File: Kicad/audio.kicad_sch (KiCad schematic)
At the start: 39 parts, among them J801 Conn_01x04, J802 Conn_02x05, J803 Conn_01x04, U801 TLV320AIC23BPW, U802 STX-4335-5BGP-S1, Y801 12M 20pF

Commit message: Label adjustments.
Swap 10uF to 10u (the F is implied)
Adjust some left/right alignment and nudge some labels around
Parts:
- C801, C808, C809: value 100uF -> 100u
- C802, C803, C806, C807, C815: value 10uF -> 10u
- C804, C805, C810, C811, C818: value 1uF -> 1u
- C812, C813, C819: value 47pF -> 47p
- C814: value 100nF -> 100n
- C816, C817: value 22pF -> 22p
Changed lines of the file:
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@@
       (effects (font (size 1.27 1.27)) (justify left))
     )
-    (property "Value" "10uF" (id 1) (at 64.135 33.02 0)
+    (property "Value" "10u" (id 1) (at 64.135 33.02 0)
       (effects (font (size 1.27 1.27)) (justify left))
     )
@@
       (effects (font (size 1.27 1.27)) (justify left))
     )
-    (property "Value" "10uF" (id 1) (at 52.705 33.02 0)
+    (property "Value" "10u" (id 1) (at 52.705 33.02 0)
       (effects (font (size 1.27 1.27)) (justify left))
     )
@@
       (effects (font (size 1.27 1.27)) (justify left))
     )
-    (property "Value" "10uF" (id 1) (at 42.291 52.578 0)
+    (property "Value" "10u" (id 1) (at 42.291 52.578 0)
       (effects (font (size 1.27 1.27)) (justify left))
     )
@@
       (effects (font (size 1.27 1.27)) (justify left))
     )
-    (property "Value" "10uF" (id 1) (at 104.14 111.76 0)
+    (property "Value" "10u" (id 1) (at 104.14 111.76 0)
       (effects (font (size 1.27 1.27)) (justify left))
     )
@@
       (effects (font (size 1.27 1.27)) (justify left))
     )
-    (property "Value" "100nF" (id 1) (at 92.71 111.76 0)
+    (property "Value" "100n" (id 1) (at 92.71 111.76 0)
       (effects (font (size 1.27 1.27)) (justify left))
     )
@@
       (effects (font (size 1.27 1.27)) (justify right))
     )
-    (property "Value" "22pF" (id 1) (at 36.83 121.285 0)
+    (property "Value" "22p" (id 1) (at 36.83 121.285 0)
       (effects (font (size 1.27 1.27)) (justify right))
     )
@@
       (effects (font (size 1.27 1.27)) (justify left))
     )
-    (property "Value" "22pF" (id 1) (at 48.26 121.285 0)
+    (property "Value" "22p" (id 1) (at 48.26 121.285 0)
       (effects (font (size 1.27 1.27)) (justify left))
     )
@@
     (in_bom yes) (on_board yes)
     (property "Reference" "C808" (id 0) (at 134.62 56.515 90))
-    (property "Value" "100uF" (id 1) (at 134.62 58.8264 90))
+    (property "Value" "100u" (id 1) (at 134.62 58.8264 90))
     (property "Footprint" "Capacitor_THT:CP_Radial_D8.0mm_P5.00mm" (id 2) (at 134.62 62.23 0)
       (effects (font (size 1.27 1.27)) hide)
@@
       (effects (font (size 1.27 1.27)) (justify right))
     )
-    (property "Value" "47pF" (id 1) (at 184.5818 128.778 0)
+    (property "Value" "47p" (id 1) (at 184.5818 128.778 0)
       (effects (font (size 1.27 1.27)) (justify right))
     )
@@
     (in_bom yes) (on_board yes)
     (property "Reference" "C818" (id 0) (at 158.75 127 90))
-    (property "Value" "1uF" (id 1) (at 158.75 129.54 90))
+    (property "Value" "1u" (id 1) (at 158.75 129.54 90))
     (property "Footprint" "Capacitor_SMD:C_0805_2012Metric_Pad1.18x1.45mm_HandSolder" (id 2) (at 158.75 123.19 0)
       (effects (font (size 1.27 1.27)) hide)
@@
     (in_bom yes) (on_board yes)
     (property "Reference" "C811" (id 0) (at 134.62 99.06 90))
-    (property "Value" "1uF" (id 1) (at 134.62 101.6 90))
+    (property "Value" "1u" (id 1) (at 134.62 101.6 90))
     (property "Footprint" "Capacitor_SMD:C_0805_2012Metric_Pad1.18x1.45mm_HandSolder" (id 2) (at 134.62 95.25 0)
       (effects (font (size 1.27 1.27)) hide)
@@
     (in_bom yes) (on_board yes)
     (property "Reference" "C805" (id 0) (at 134.62 41.91 90))
-    (property "Value" "1uF" (id 1) (at 134.62 39.37 90))
+    (property "Value" "1u" (id 1) (at 134.62 39.37 90))
     (property "Footprint" "Capacitor_SMD:C_0805_2012Metric_Pad1.18x1.45mm_HandSolder" (id 2) (at 134.62 35.56 0)
       (effects (font (size 1.27 1.27)) hide)
@@
       (effects (font (size 1.27 1.27)) (justify right))
     )
-    (property "Value" "47pF" (id 1) (at 157.2768 100.203 0)
+    (property "Value" "47p" (id 1) (at 157.2768 100.203 0)
       (effects (font (size 1.27 1.27)) (justify right))
     )
@@
       (effects (font (size 1.27 1.27)) (justify right))
     )
-    (property "Value" "47pF" (id 1) (at 147.7518 100.203 0)
+    (property "Value" "47p" (id 1) (at 147.7518 100.203 0)
       (effects (font (size 1.27 1.27)) (justify right))
     )
@@
       (effects (font (size 1.27 1.27)) (justify left))
     )
-    (property "Value" "100uF" (id 1) (at 41.275 33.02 0)
+    (property "Value" "100u" (id 1) (at 41.275 33.02 0)
       (effects (font (size 1.27 1.27)) (justify left))
     )
@@
     (in_bom yes) (on_board yes)
     (property "Reference" "C809" (id 0) (at 134.62 71.755 90))
-    (property "Value" "100uF" (id 1) (at 134.62 69.215 90))
+    (property "Value" "100u" (id 1) (at 134.62 69.215 90))
     (property "Footprint" "Capacitor_THT:CP_Radial_D8.0mm_P5.00mm" (id 2) (at 134.62 66.04 0)
       (effects (font (size 1.27 1.27)) hide)
@@
     (in_bom yes) (on_board yes)
     (property "Reference" "C810" (id 0) (at 134.62 86.36 90))
-    (property "Value" "1uF" (id 1) (at 134.62 88.265 90))
+    (property "Value" "1u" (id 1) (at 134.62 88.265 90))
     (property "Footprint" "Capacitor_SMD:C_0805_2012Metric_Pad1.18x1.45mm_HandSolder" (id 2) (at 134.62 91.44 0)
       (effects (font (size 1.27 1.27)) hide)
@@
     (in_bom yes) (on_board yes)
     (property "Reference" "C804" (id 0) (at 134.62 25.4 90))
-    (property "Value" "1uF" (id 1) (at 134.62 27.94 90))
+    (property "Value" "1u" (id 1) (at 134.62 27.94 90))
     (property "Footprint" "Capacitor_SMD:C_0805_2012Metric_Pad1.18x1.45mm_HandSolder" (id 2) (at 134.62 31.75 0)
       (effects (font (size 1.27 1.27)) hide)
@@
       (effects (font (size 1.27 1.27)) (justify left))
     )
-    (property "Value" "10uF" (id 1) (at 53.086 52.578 0)
-      (effects (font (size 1.27 1.27)) (justify left))
-    )
+    (property "Value" "10u" (id 1) (at 53.086 52.578 0)
+      (effects (font (size 1.27 1.27)) (justify left))
+    )

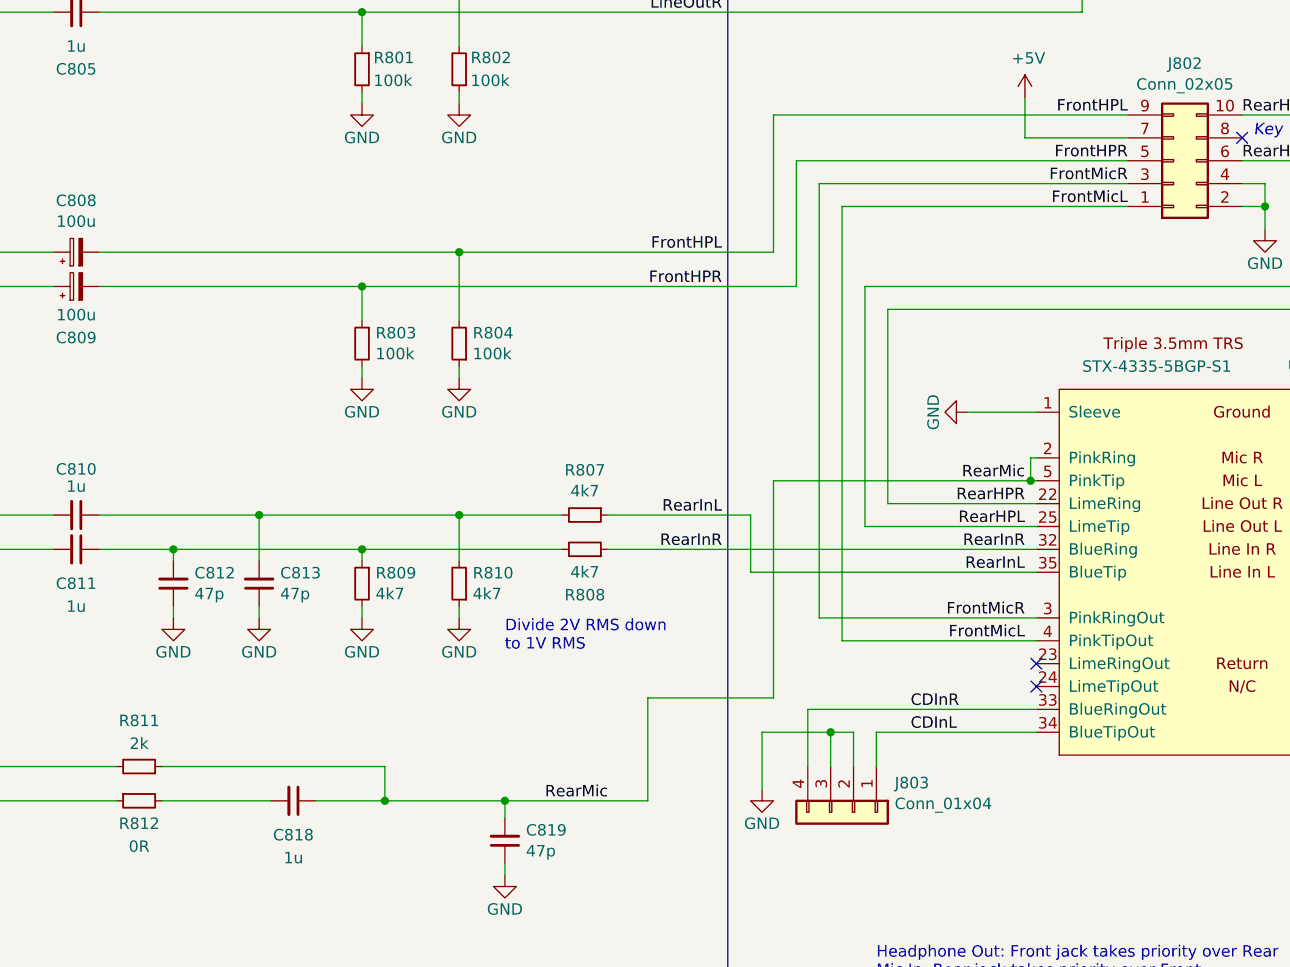
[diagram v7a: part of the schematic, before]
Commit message: Fix mic/bias circuit.
Also:

* added MOV as 3D model for fuse
* re-routed bottom side 5V line
* added some GND vias near power vias to reduce loop area
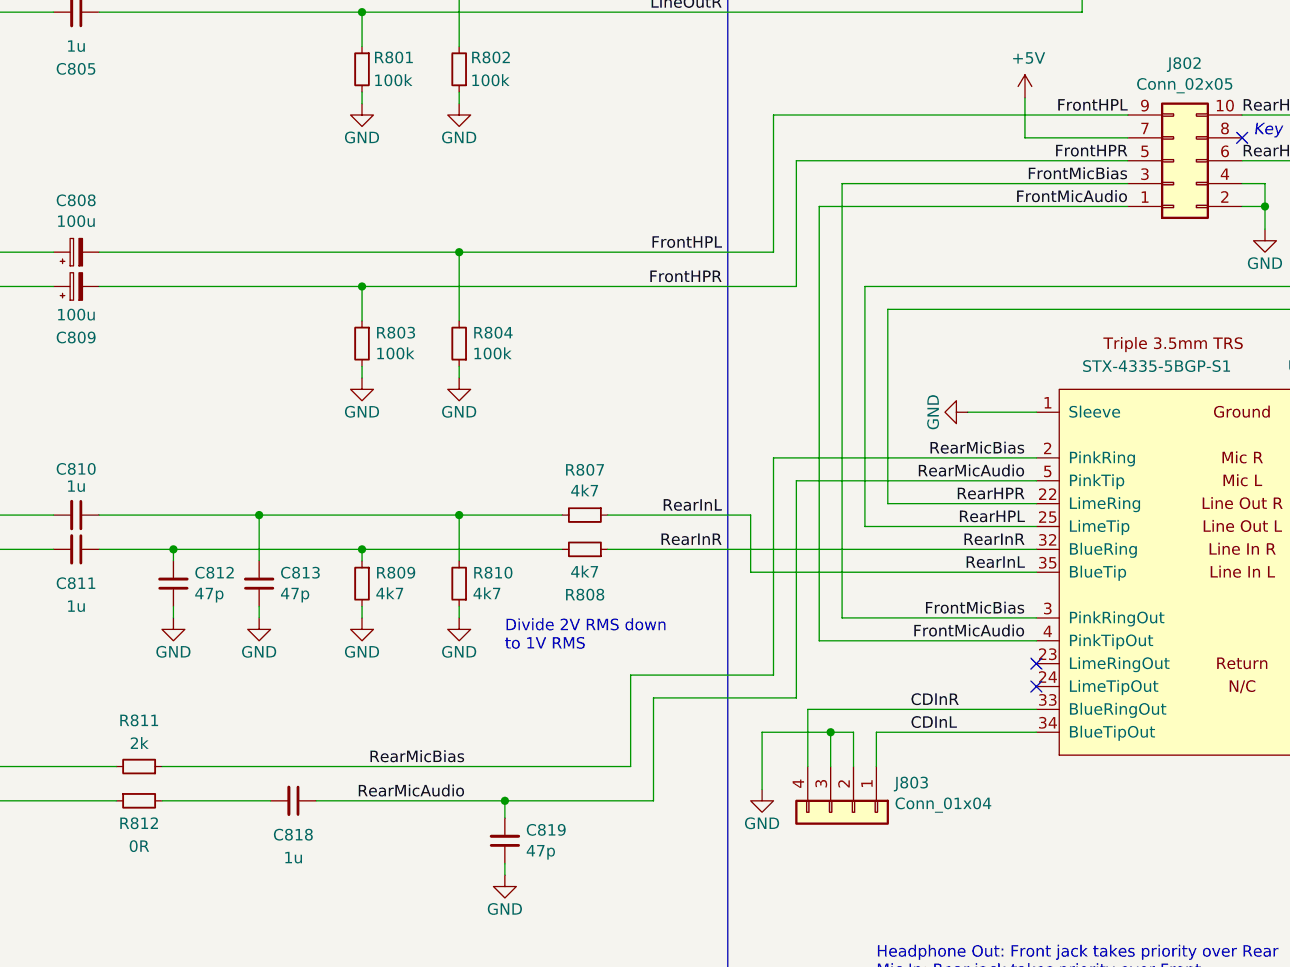
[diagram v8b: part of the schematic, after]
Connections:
- net FrontMicL renamed FrontMicAudio
- net FrontMicR renamed FrontMicBias
- net RearMic renamed RearMicAudio
- net RearMicAudio: no longer R811.1, U802.2 (PinkRing)
- new net RearMicBias: R811.1, U802.2 (PinkRing)
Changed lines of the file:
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@@
   (junction (at 266.7 57.15) (diameter 0) (color 0 0 0 0)
   )
-  (junction (at 240.665 87.63) (diameter 0) (color 0 0 0 0)
-  )
   (junction (at 60.96 60.96) (diameter 0) (color 0 0 0 0)
-  )
-  (junction (at 168.91 123.19) (diameter 0) (color 0 0 0 0)
   )
   (junction (at 177.165 91.44) (diameter 0) (color 0 0 0 0)
@@
     (stroke (width 0) (type default) (color 0 0 0 0))
   )
-  (wire (pts (xy 219.71 57.15) (xy 251.46 57.15))
-    (stroke (width 0) (type default) (color 0 0 0 0))
-  )
-  (wire (pts (xy 217.17 102.87) (xy 241.3 102.87))
+  (wire (pts (xy 217.17 57.15) (xy 251.46 57.15))
+    (stroke (width 0) (type default) (color 0 0 0 0))
+  )
+  (wire (pts (xy 219.71 102.87) (xy 241.3 102.87))
     (stroke (width 0) (type default) (color 0 0 0 0))
   )
@@
     (stroke (width 0) (type default) (color 0 0 0 0))
   )
-  (wire (pts (xy 219.71 105.41) (xy 241.3 105.41))
+  (wire (pts (xy 217.17 105.41) (xy 241.3 105.41))
     (stroke (width 0) (type default) (color 0 0 0 0))
   )
@@
     (stroke (width 0) (type default) (color 0 0 0 0))
   )
-  (wire (pts (xy 144.145 119.38) (xy 168.91 119.38))
-    (stroke (width 0) (type default) (color 0 0 0 0))
-  )
   (wire (pts (xy 39.37 56.515) (xy 39.37 55.245))
     (stroke (width 0) (type default) (color 0 0 0 0))
@@
     (stroke (width 0) (type default) (color 0 0 0 0))
   )
-  (wire (pts (xy 212.09 111.76) (xy 198.12 111.76))
+  (wire (pts (xy 214.63 111.76) (xy 198.755 111.76))
     (stroke (width 0) (type default) (color 0 0 0 0))
   )
@@
     (stroke (width 0) (type default) (color 0 0 0 0))
   )
-  (wire (pts (xy 240.665 87.63) (xy 241.3 87.63))
-    (stroke (width 0) (type default) (color 0 0 0 0))
-  )
-  (wire (pts (xy 217.17 54.61) (xy 251.46 54.61))
+  (wire (pts (xy 219.71 54.61) (xy 251.46 54.61))
+    (stroke (width 0) (type default) (color 0 0 0 0))
+  )
+  (wire (pts (xy 212.09 85.09) (xy 212.09 109.22))
     (stroke (width 0) (type default) (color 0 0 0 0))
   )
@@
     (stroke (width 0) (type default) (color 0 0 0 0))
   )
-  (wire (pts (xy 212.09 87.63) (xy 240.665 87.63))
+  (wire (pts (xy 214.63 87.63) (xy 241.3 87.63))
     (stroke (width 0) (type default) (color 0 0 0 0))
   )
@@
     (stroke (width 0) (type default) (color 0 0 0 0))
   )
-  (wire (pts (xy 168.91 119.38) (xy 168.91 123.19))
+  (wire (pts (xy 241.3 85.09) (xy 212.09 85.09))
     (stroke (width 0) (type default) (color 0 0 0 0))
   )
@@
     (stroke (width 0) (type default) (color 0 0 0 0))
   )
-  (wire (pts (xy 217.17 54.61) (xy 217.17 102.87))
+  (wire (pts (xy 219.71 54.61) (xy 219.71 102.87))
     (stroke (width 0) (type default) (color 0 0 0 0))
   )
@@
     (stroke (width 0) (type default) (color 0 0 0 0))
   )
-  (wire (pts (xy 240.665 85.09) (xy 240.665 87.63))
-    (stroke (width 0) (type default) (color 0 0 0 0))
-  )
   (wire (pts (xy 264.16 46.99) (xy 280.67 46.99))
     (stroke (width 0) (type default) (color 0 0 0 0))
@@
     (stroke (width 0) (type default) (color 0 0 0 0))
   )
+  (wire (pts (xy 144.145 119.38) (xy 196.215 119.38))
+    (stroke (width 0) (type default) (color 0 0 0 0))
+  )
   (wire (pts (xy 166.37 95.25) (xy 188.595 95.25))
     (stroke (width 0) (type default) (color 0 0 0 0))
@@
     (stroke (width 0) (type default) (color 0 0 0 0))
   )
-  (wire (pts (xy 161.29 123.19) (xy 168.91 123.19))
-    (stroke (width 0) (type default) (color 0 0 0 0))
-  )
   (wire (pts (xy 39.37 47.625) (xy 39.37 45.72))
     (stroke (width 0) (type default) (color 0 0 0 0))
@@
     (stroke (width 0) (type default) (color 0 0 0 0))
   )
-  (wire (pts (xy 168.91 123.19) (xy 182.245 123.19))
+  (wire (pts (xy 161.29 123.19) (xy 182.245 123.19))
     (stroke (width 0) (type default) (color 0 0 0 0))
   )
@@
     (stroke (width 0) (type default) (color 0 0 0 0))
   )
-  (wire (pts (xy 198.12 111.76) (xy 198.12 123.19))
+  (wire (pts (xy 198.755 111.76) (xy 198.755 123.19))
     (stroke (width 0) (type default) (color 0 0 0 0))
   )
@@
     (stroke (width 0) (type default) (color 0 0 0 0))
   )
-  (wire (pts (xy 212.09 87.63) (xy 212.09 111.76))
+  (wire (pts (xy 214.63 87.63) (xy 214.63 111.76))
     (stroke (width 0) (type default) (color 0 0 0 0))
   )
@@
     (stroke (width 0) (type default) (color 0 0 0 0))
   )
+  (wire (pts (xy 212.09 109.22) (xy 196.215 109.22))
+    (stroke (width 0) (type default) (color 0 0 0 0))
+  )
   (wire (pts (xy 166.37 101.6) (xy 166.37 102.87))
     (stroke (width 0) (type default) (color 0 0 0 0))
@@
     (stroke (width 0) (type default) (color 0 0 0 0))
   )
+  (wire (pts (xy 196.215 109.22) (xy 196.215 119.38))
+    (stroke (width 0) (type default) (color 0 0 0 0))
+  )
   (wire (pts (xy 214.63 52.07) (xy 214.63 66.04))
     (stroke (width 0) (type default) (color 0 0 0 0))
@@
     (stroke (width 0) (type default) (color 0 0 0 0))
   )
-  (wire (pts (xy 240.665 85.09) (xy 241.3 85.09))
-    (stroke (width 0) (type default) (color 0 0 0 0))
-  )
   (wire (pts (xy 107.95 62.23) (xy 107.95 78.74))
     (stroke (width 0) (type default) (color 0 0 0 0))
@@
     (stroke (width 0) (type default) (color 0 0 0 0))
   )
-  (wire (pts (xy 219.71 105.41) (xy 219.71 57.15))
+  (wire (pts (xy 217.17 105.41) (xy 217.17 57.15))
     (stroke (width 0) (type default) (color 0 0 0 0))
   )
@@
     (stroke (width 0) (type default) (color 0 0 0 0))
   )
-  (wire (pts (xy 182.245 123.19) (xy 198.12 123.19))
+  (wire (pts (xy 182.245 123.19) (xy 198.755 123.19))
     (stroke (width 0) (type default) (color 0 0 0 0))
   )
@@
     (effects (font (size 1.27 1.27)) (justify right bottom))
   )
-  (label "RearMic" (at 186.69 123.19 0)
-    (effects (font (size 1.27 1.27)) (justify left bottom))
-  )
-  (label "FrontMicR" (at 251.46 54.61 180)
+  (label "FrontMicBias" (at 251.46 54.61 180)
     (effects (font (size 1.27 1.27)) (justify right bottom))
   )
@@
     (effects (font (size 1.27 1.27)) (justify right bottom))
   )
-  (label "RearMic" (at 240.03 87.63 180)
-    (effects (font (size 1.27 1.27)) (justify right bottom))
-  )
-  (label "FrontMicR" (at 240.03 102.87 180)
+  (label "RearMicAudio" (at 240.03 87.63 180)
+    (effects (font (size 1.27 1.27)) (justify right bottom))
+  )
+  (label "FrontMicBias" (at 240.03 102.87 180)
     (effects (font (size 1.27 1.27)) (justify right bottom))
   )
@@
     (effects (font (size 1.27 1.27)) (justify left bottom))
   )
-  (label "FrontMicL" (at 240.03 105.41 180)
+  (label "FrontMicAudio" (at 240.03 105.41 180)
     (effects (font (size 1.27 1.27)) (justify right bottom))
   )
@@
     (effects (font (size 1.27 1.27)) (justify right bottom))
   )
+  (label "RearMicBias" (at 177.8 119.38 180)
+    (effects (font (size 1.27 1.27)) (justify right bottom))
+  )
   (label "MicBias" (at 119.38 119.38 0)
     (effects (font (size 1.27 1.27)) (justify left bottom))
@@
     (effects (font (size 1.27 1.27)) (justify left bottom))
   )
-  (label "FrontMicL" (at 251.46 57.15 180)
+  (label "FrontMicAudio" (at 251.46 57.15 180)
     (effects (font (size 1.27 1.27)) (justify right bottom))
   )
@@
     (effects (font (size 1.27 1.27)) (justify right bottom))
   )
+  (label "RearMicBias" (at 240.03 85.09 180)
+    (effects (font (size 1.27 1.27)) (justify right bottom))
+  )
   (label "RearHPL" (at 264.16 46.99 0)
     (effects (font (size 1.27 1.27)) (justify left bottom))
   )
+  (label "RearMicAudio" (at 177.8 123.19 180)
+    (effects (font (size 1.27 1.27)) (justify right bottom))
+  )
   (label "LOut" (at 108.585 31.75 0)
